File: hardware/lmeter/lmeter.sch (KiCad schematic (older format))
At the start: 13 parts, among them J1 Conn_01x08, U1 LM324

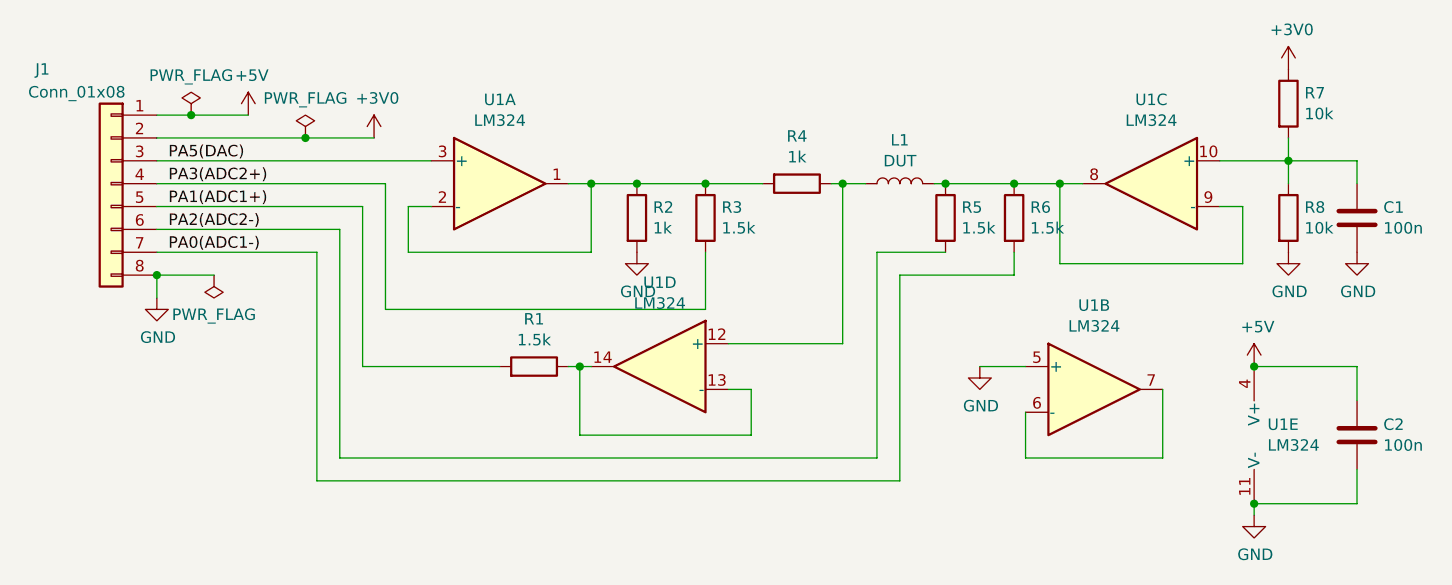
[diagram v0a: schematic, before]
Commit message: hardware: remove 1.5k resistors
Remove the 1.5k resistors between the op amp outputs and ADC inputs.
While the datasheets say they should be fine, they lead to small amounts
of error.
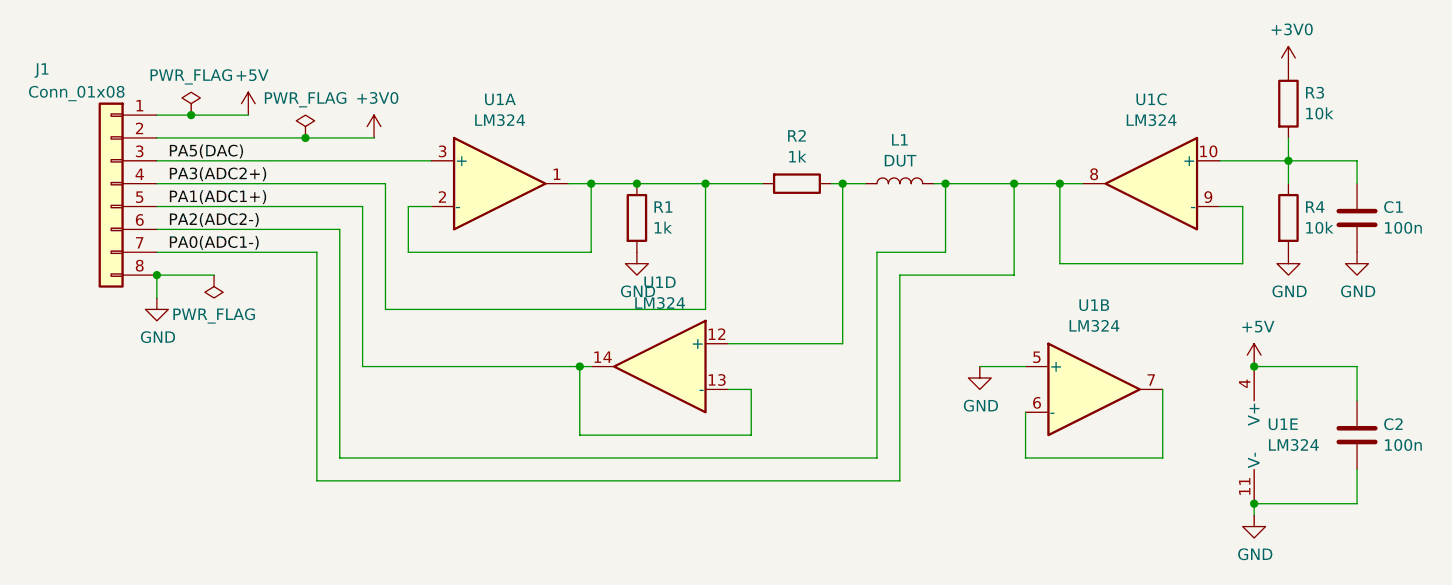
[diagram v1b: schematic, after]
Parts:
- removed R1, R3, R5, R6: 1.5k, symbol Device:R
- renumbered R2 to R1, R4 to R2, R7 to R3, R8 to R4
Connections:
- net PA2(ADC2-) is gone; now on net PA0(ADC1-): J1.6 (Pin_6)
- net PA0(ADC1-): now also L1.2, U1.8, U1.9 (-)
- net PA1(ADC1+): now also U1.13 (-), U1.14
- net PA3(ADC2+): now also R1.1, R2.2, U1.1, U1.2 (-)
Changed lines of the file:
@@
 $EndComp
 $Comp
-L Device:R R4
+L Device:R R2
 U 1 1 5EFD6FEC
 P 5700 3400
-F 0 "R4" V 5493 3400 50  0000 C CNN
+F 0 "R2" V 5493 3400 50  0000 C CNN
 F 1 "1k" V 5584 3400 50  0000 C CNN
 F 2 "" V 5630 3400 50  0001 C CNN
@@
 $EndComp
 $Comp
-L Device:R R3
-U 1 1 5EFDC46B
-P 5300 3550
-F 0 "R3" H 5370 3596 50  0000 L CNN
-F 1 "1.5k" H 5370 3505 50  0000 L CNN
-F 2 "" V 5230 3550 50  0001 C CNN
-F 3 "~" H 5300 3550 50  0001 C CNN
-	1    5300 3550
-	1    0    0    -1
-$EndComp
-Connection ~ 5300 3400
-$Comp
-L Device:R R2
+L Device:R R1
 U 1 1 5EFDC735
 P 5000 3550
-F 0 "R2" H 5070 3596 50  0000 L CNN
+F 0 "R1" H 5070 3596 50  0000 L CNN
 F 1 "1k" H 5070 3505 50  0000 L CNN
 F 2 "" V 4930 3550 50  0001 C CNN
@@
 $EndComp
 Connection ~ 5000 3400
-Wire Wire Line
-	5000 3400 5300 3400
 $Comp
 L Device:L L1
@@
 Wire Wire Line
 	5850 3400 5900 3400
-Wire Wire Line
-	6300 3400 6350 3400
 $Comp
 L Amplifier_Operational:LM324 U1
@@
 	5900 3400 6000 3400
 $Comp
-L Device:R R5
-U 1 1 5EFE17A2
-P 6350 3550
-F 0 "R5" H 6420 3596 50  0000 L CNN
-F 1 "1.5k" H 6420 3505 50  0000 L CNN
-F 2 "" V 6280 3550 50  0001 C CNN
-F 3 "~" H 6350 3550 50  0001 C CNN
-	1    6350 3550
-	1    0    0    -1
-$EndComp
-Connection ~ 6350 3400
-$Comp
-L Device:R R6
-U 1 1 5EFE26E2
-P 6650 3550
-F 0 "R6" H 6720 3596 50  0000 L CNN
-F 1 "1.5k" H 6720 3505 50  0000 L CNN
-F 2 "" V 6580 3550 50  0001 C CNN
-F 3 "~" H 6650 3550 50  0001 C CNN
-	1    6650 3550
-	1    0    0    -1
-$EndComp
-Connection ~ 6650 3400
-Wire Wire Line
-	6650 3400 6850 3400
-$Comp
-L power:GND #PWR0101
+L power:GND #PWR04
 U 1 1 5EFE2C8B
 P 5000 3700
-F 0 "#PWR0101" H 5000 3450 50  0001 C CNN
+F 0 "#PWR04" H 5000 3450 50  0001 C CNN
 F 1 "GND" H 5005 3527 50  0000 C CNN
 F 2 "" H 5000 3700 50  0001 C CNN
@@
 	5500 4500 4750 4500
 Connection ~ 4750 4200
-Wire Wire Line
-	4750 4200 4700 4200
-$Comp
-L Device:R R7
+$Comp
+L Device:R R3
 U 1 1 5EFEB053
 P 7850 3050
-F 0 "R7" H 7920 3096 50  0000 L CNN
+F 0 "R3" H 7920 3096 50  0000 L CNN
 F 1 "10k" H 7920 3005 50  0000 L CNN
 F 2 "" V 7780 3050 50  0001 C CNN
@@
 $EndComp
 $Comp
-L Device:R R8
+L Device:R R4
 U 1 1 5EFEB785
 P 7850 3550
-F 0 "R8" H 7920 3596 50  0000 L CNN
+F 0 "R4" H 7920 3596 50  0000 L CNN
 F 1 "10k" H 7920 3505 50  0000 L CNN
 F 2 "" V 7780 3550 50  0001 C CNN
@@
 	8150 3300 8150 3400
 $Comp
-L power:GND #PWR0102
+L power:GND #PWR09
 U 1 1 5EFEF733
 P 7850 3700
-F 0 "#PWR0102" H 7850 3450 50  0001 C CNN
+F 0 "#PWR09" H 7850 3450 50  0001 C CNN
 F 1 "GND" H 7855 3527 50  0000 C CNN
 F 2 "" H 7850 3700 50  0001 C CNN
@@
 $EndComp
 $Comp
-L power:GND #PWR0103
+L power:GND #PWR010
 U 1 1 5EFF0513
 P 8150 3700
-F 0 "#PWR0103" H 8150 3450 50  0001 C CNN
+F 0 "#PWR010" H 8150 3450 50  0001 C CNN
 F 1 "GND" H 8155 3527 50  0000 C CNN
 F 2 "" H 8150 3700 50  0001 C CNN
@@
 $EndComp
 $Comp
-L power:GND #PWR0104
+L power:GND #PWR07
 U 1 1 5EFF1A46
 P 7700 4850
-F 0 "#PWR0104" H 7700 4600 50  0001 C CNN
+F 0 "#PWR07" H 7700 4600 50  0001 C CNN
 F 1 "GND" H 7705 4677 50  0000 C CNN
 F 2 "" H 7700 4850 50  0001 C CNN
@@
 	2900 3300 4100 3300
 $Comp
-L power:+5V #PWR0105
+L power:+5V #PWR02
 U 1 1 5EFF8B8A
 P 3300 3100
-F 0 "#PWR0105" H 3300 2950 50  0001 C CNN
+F 0 "#PWR02" H 3300 2950 50  0001 C CNN
 F 1 "+5V" H 3315 3273 50  0000 C CNN
 F 2 "" H 3300 3100 50  0001 C CNN
@@
 	2900 3100 3050 3100
 $Comp
-L power:+3V0 #PWR0106
+L power:+3V0 #PWR03
 U 1 1 5EFFB0D8
 P 3850 3200
-F 0 "#PWR0106" H 3850 3050 50  0001 C CNN
+F 0 "#PWR03" H 3850 3050 50  0001 C CNN
 F 1 "+3V0" H 3865 3373 50  0000 C CNN
 F 2 "" H 3850 3200 50  0001 C CNN
@@
 	3850 3200 3550 3200
 $Comp
-L power:GND #PWR0107
+L power:GND #PWR01
 U 1 1 5EFFC310
 P 2900 3900
-F 0 "#PWR0107" H 2900 3650 50  0001 C CNN
+F 0 "#PWR01" H 2900 3650 50  0001 C CNN
 F 1 "GND" H 2905 3727 50  0000 C CNN
 F 2 "" H 2900 3900 50  0001 C CNN
@@
 	2900 3900 2900 3800
 $Comp
-L power:+5V #PWR0108
+L power:+5V #PWR06
 U 1 1 5EFFD492
 P 7700 4200
-F 0 "#PWR0108" H 7700 4050 50  0001 C CNN
+F 0 "#PWR06" H 7700 4050 50  0001 C CNN
 F 1 "+5V" H 7715 4373 50  0000 C CNN
 F 2 "" H 7700 4200 50  0001 C CNN
@@
 $EndComp
 $Comp
-L power:+3V0 #PWR0109
+L power:+3V0 #PWR08
 U 1 1 5EFFDD42
 P 7850 2900
-F 0 "#PWR0109" H 7850 2750 50  0001 C CNN
+F 0 "#PWR08" H 7850 2750 50  0001 C CNN
 F 1 "+3V0" H 7865 3073 50  0000 C CNN
 F 2 "" H 7850 2900 50  0001 C CNN
@@
 PA5(DAC)
 Wire Wire Line
-	5300 3400 5550 3400
-Wire Wire Line
 	2900 3400 3900 3400
 Wire Wire Line
@@
 	3900 3950 5300 3950
 Wire Wire Line
-	5300 3950 5300 3700
-Wire Wire Line
-	6350 3400 6650 3400
-Wire Wire Line
 	7300 4600 7300 4300
 $Comp
-L Device:R R1
-U 1 1 5EFE86C1
-P 4550 4200
-F 0 "R1" V 4757 4200 50  0000 C CNN
-F 1 "1.5k" V 4666 4200 50  0000 C CNN
-F 2 "" V 4480 4200 50  0001 C CNN
-F 3 "~" H 4550 4200 50  0001 C CNN
-	1    4550 4200
-	0    1    -1   0
-$EndComp
-$Comp
-L power:GND #PWR0110
+L power:GND #PWR05
 U 1 1 5EFE7D60
 P 6500 4200
-F 0 "#PWR0110" H 6500 3950 50  0001 C CNN
+F 0 "#PWR05" H 6500 3950 50  0001 C CNN
 F 1 "GND" H 6505 4027 50  0000 C CNN
 F 2 "" H 6500 4200 50  0001 C CNN
@@
 	3800 3500 3800 4200
 Wire Wire Line
-	3800 4200 4400 4200
-Wire Wire Line
 	3700 3600 3700 4600
 Wire Wire Line
@@
 Wire Wire Line
 	6050 3700 6350 3700
-Wire Wire Line
-	6650 3700 6650 3800
 Wire Wire Line
 	6650 3800 6150 3800
@@
 	8150 4800 8150 4650
 $Comp
-L power:PWR_FLAG #FLG0101
+L power:PWR_FLAG #FLG01
 U 1 1 5F0213B2
 P 3050 3100
-F 0 "#FLG0101" H 3050 3175 50  0001 C CNN
+F 0 "#FLG01" H 3050 3175 50  0001 C CNN
 F 1 "PWR_FLAG" H 3050 3273 50  0000 C CNN
 F 2 "" H 3050 3100 50  0001 C CNN
@@
 $EndComp
 $Comp
-L power:PWR_FLAG #FLG0102
+L power:PWR_FLAG #FLG03
 U 1 1 5F021999
 P 3550 3200
-F 0 "#FLG0102" H 3550 3275 50  0001 C CNN
+F 0 "#FLG03" H 3550 3275 50  0001 C CNN
 F 1 "PWR_FLAG" H 3550 3373 50  0000 C CNN
 F 2 "" H 3550 3200 50  0001 C CNN
@@
 	3550 3200 2900 3200
 $Comp
-L power:PWR_FLAG #FLG0103
+L power:PWR_FLAG #FLG02
 U 1 1 5F021B24
 P 3150 3800
-F 0 "#FLG0103" H 3150 3875 50  0001 C CNN
+F 0 "#FLG02" H 3150 3875 50  0001 C CNN
 F 1 "PWR_FLAG" H 3150 3973 50  0000 C CNN
 F 2 "" H 3150 3800 50  0001 C CNN
@@
 Connection ~ 7700 4200
 Connection ~ 7700 4800
+Wire Wire Line
+	3800 4200 4750 4200
+Wire Wire Line
+	6300 3400 6350 3400
+Wire Wire Line
+	6650 3400 6650 3800
+Connection ~ 6650 3400
+Wire Wire Line
+	6650 3400 6850 3400
+Wire Wire Line
+	6350 3700 6350 3400
+Connection ~ 6350 3400
+Wire Wire Line
+	6350 3400 6650 3400
+Wire Wire Line
+	5000 3400 5300 3400
+Connection ~ 5300 3400
+Wire Wire Line
+	5300 3400 5550 3400
+Wire Wire Line
+	5300 3400 5300 3950
 $EndSCHEMATC
